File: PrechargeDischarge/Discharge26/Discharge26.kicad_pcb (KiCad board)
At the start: 2 copper layers, 80 x 105 mm, 11 parts, among them J1 HV_Conn, J2 LV_Conn, K4 Relay_SPST-NC, Q5 NMOS

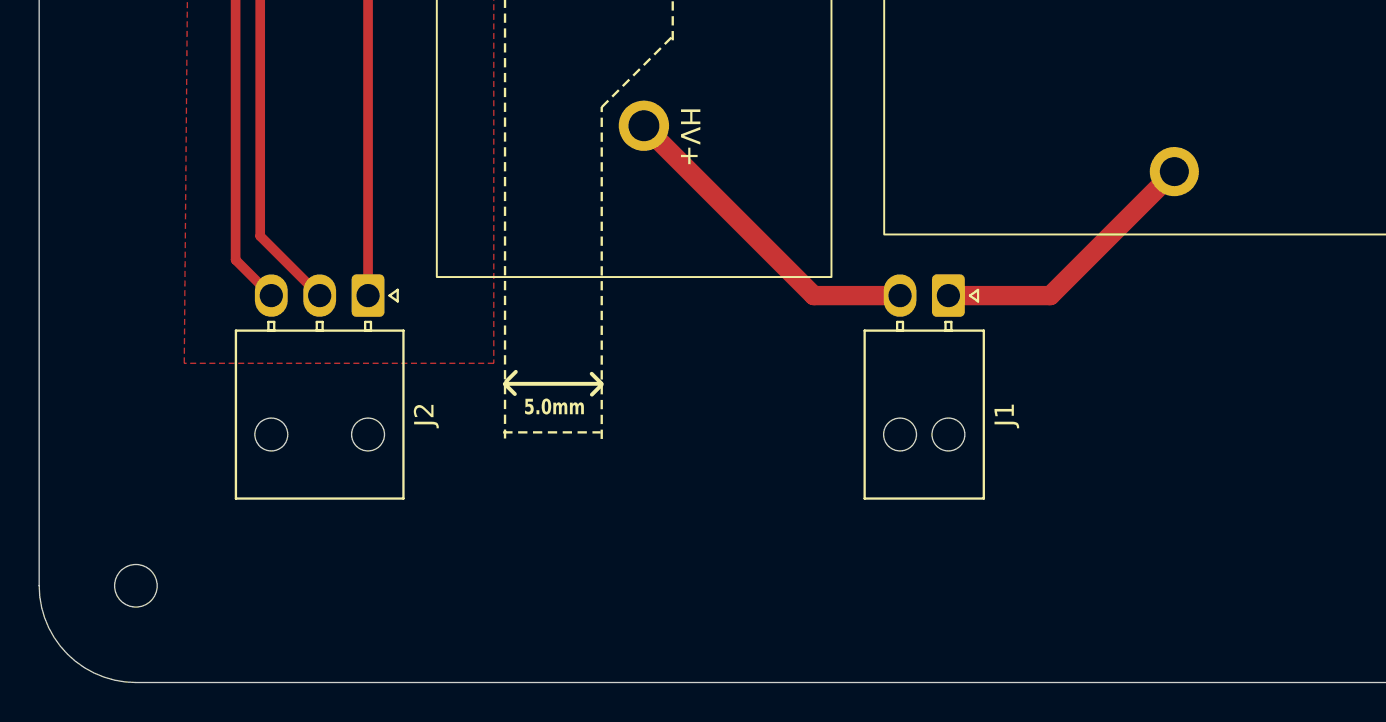
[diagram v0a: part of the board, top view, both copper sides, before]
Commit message: Precharge Testing
Uploaded precharge testing data, settled on 1.5k ohm resistor to precharge MC around 1s
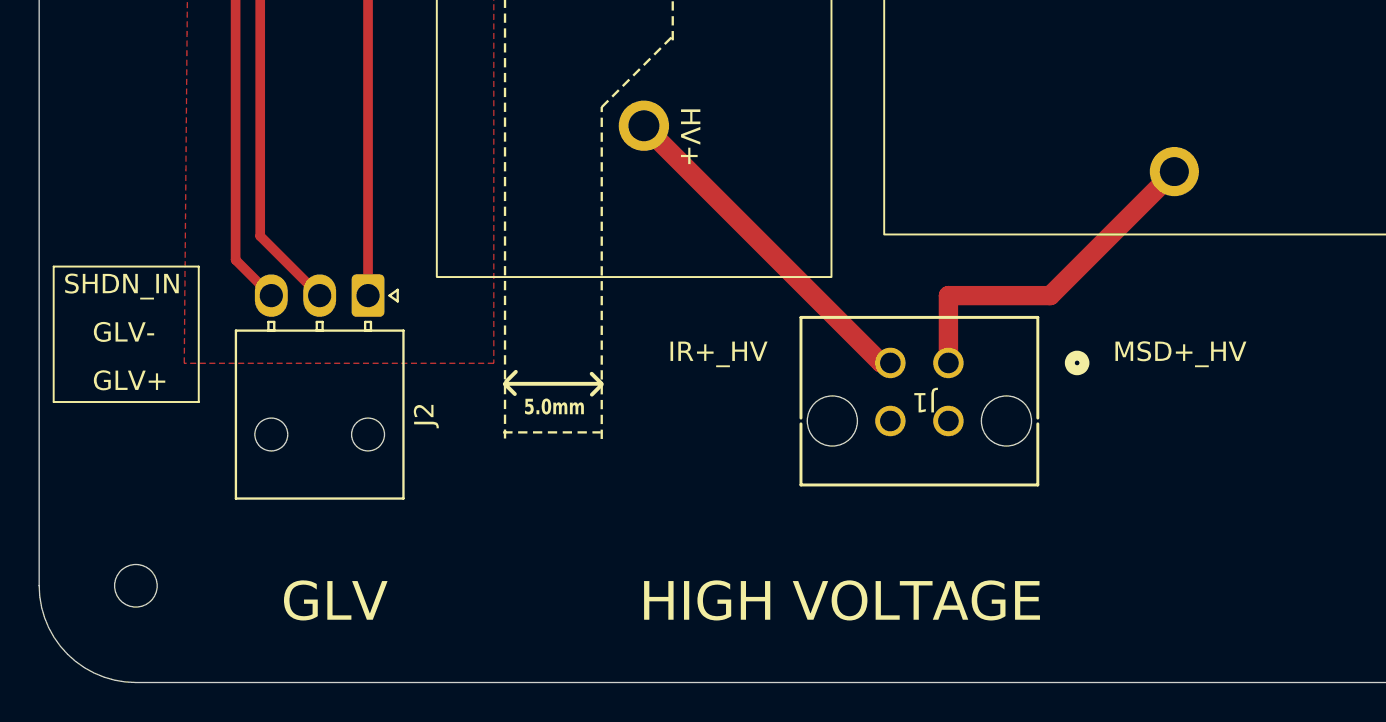
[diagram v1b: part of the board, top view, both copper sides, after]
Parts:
- J1: footprint Connector_Molex:Molex_Nano-Fit_105313-xx02_1x02_P2.50mm_Horizontal -> Discharge:MicroFit_4pin
- moved J1 5.15 mm to (170.7, 130.0), turned to 180 degrees
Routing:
- net /MSD_IN: track 14.3 -> 17.8 mm
- net /IR+: track 16.9 -> 17.8 mm
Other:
- board text added: "GLV"
- board text added: "GLV+"
- board text added: "GLV-"
- board text added: "HIGH VOLTAGE"
- board text added: "IR+_HV"
- board text added: "MSD+_HV"
- board text added: "SHDN_IN"

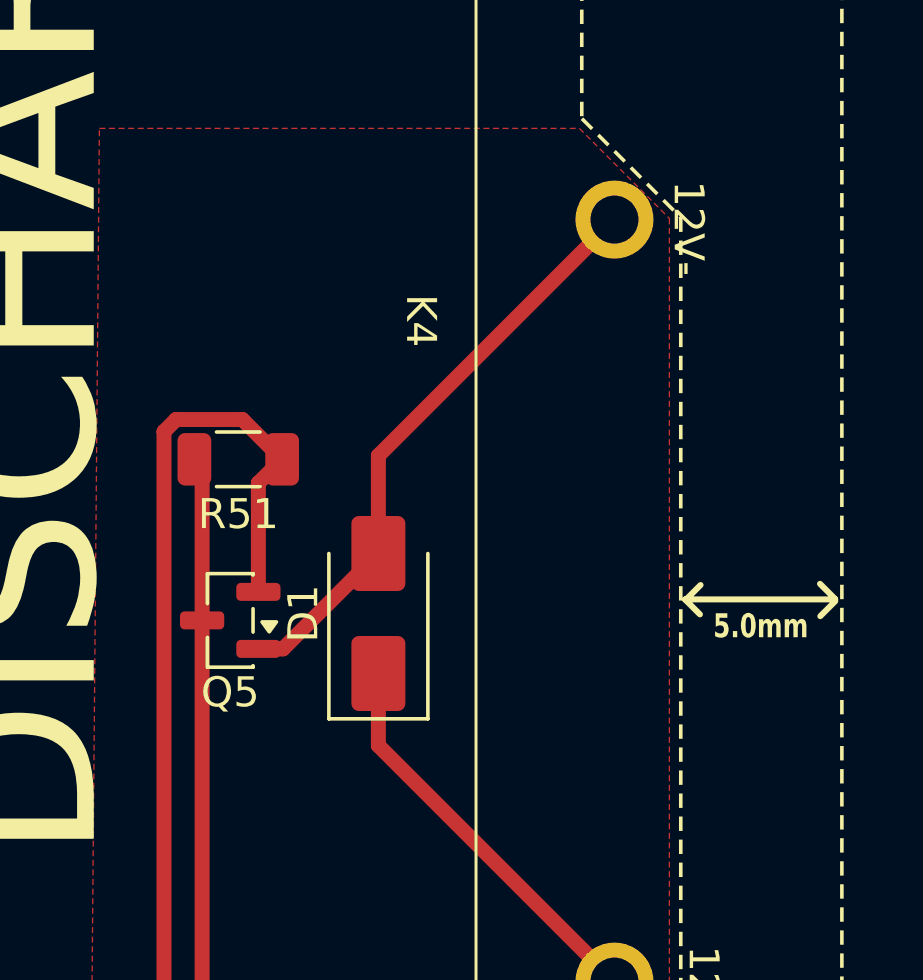
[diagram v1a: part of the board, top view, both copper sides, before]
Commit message: Discharge fixes
Fixed footprint and symbol for discharge NMOS
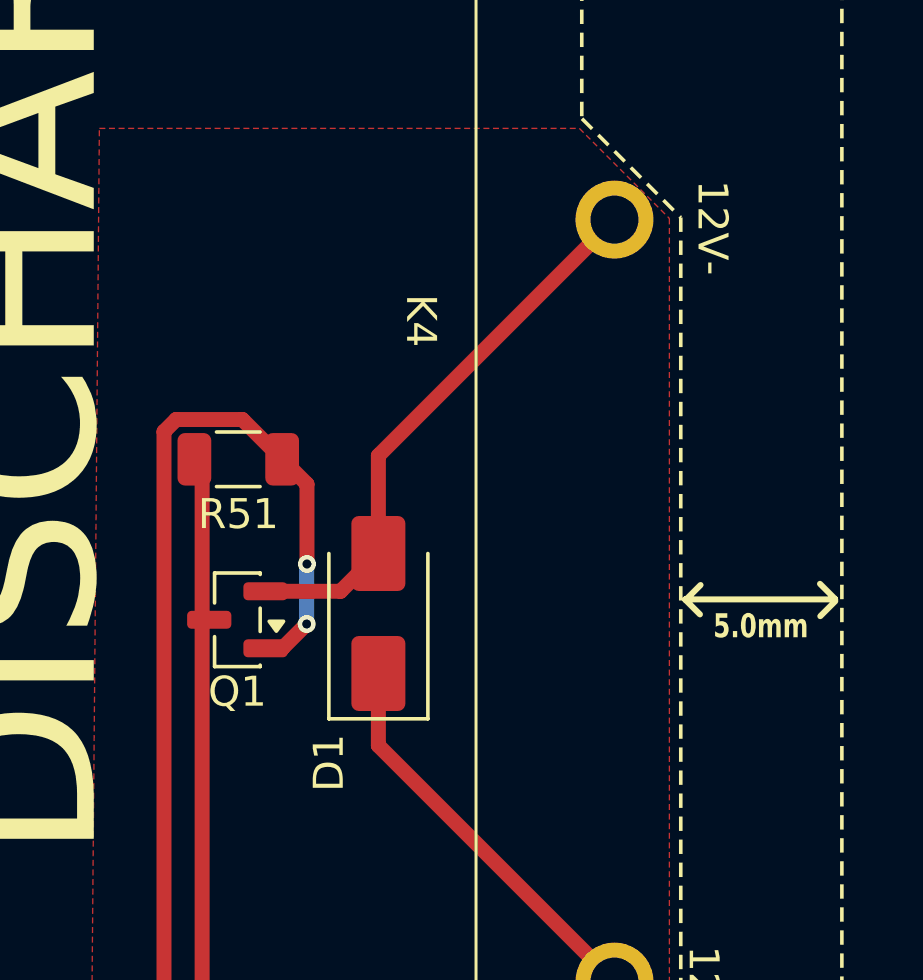
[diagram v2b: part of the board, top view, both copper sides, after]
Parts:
- removed Q5: NMOS, Package_TO_SOT_SMD:SOT-23
- added Q1: Q_NMOS_GSD, Package_TO_SOT_SMD:SOT-23, F.Cu at (137.6, 86.4)
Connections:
- J1 pad 3: (no net) -> unconnected-(J1-Pin_3-Pad3)
- J1 pad 4: (no net) -> unconnected-(J1-Pin_4-Pad4)
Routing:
- net /SHDN: track 55.1 -> 57.9 mm, vias 0 -> 2
- net Net-(D1-A): track 19.7 -> 18.7 mm

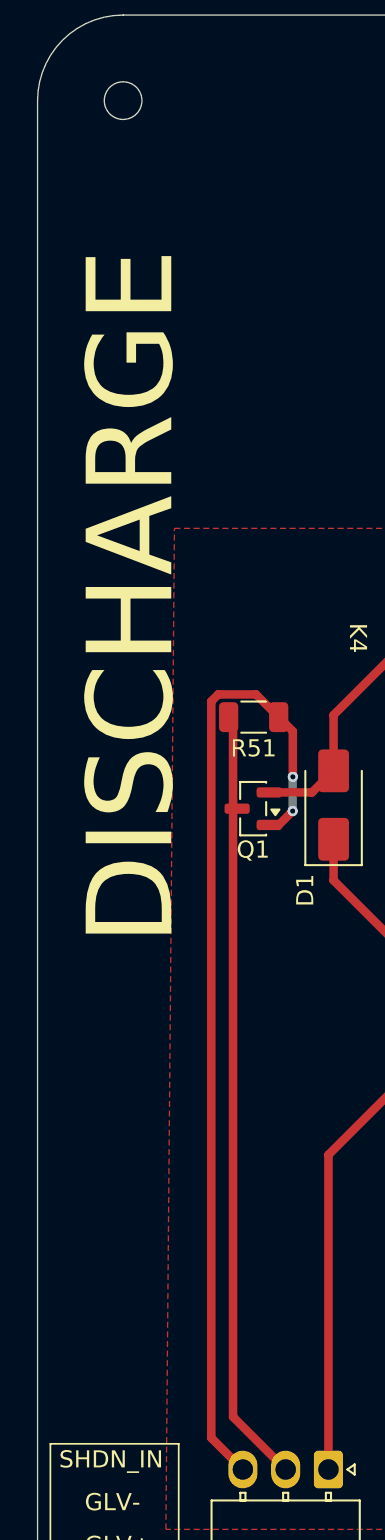
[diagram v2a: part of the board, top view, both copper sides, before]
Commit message: prechaarge
fixed precharge footprin
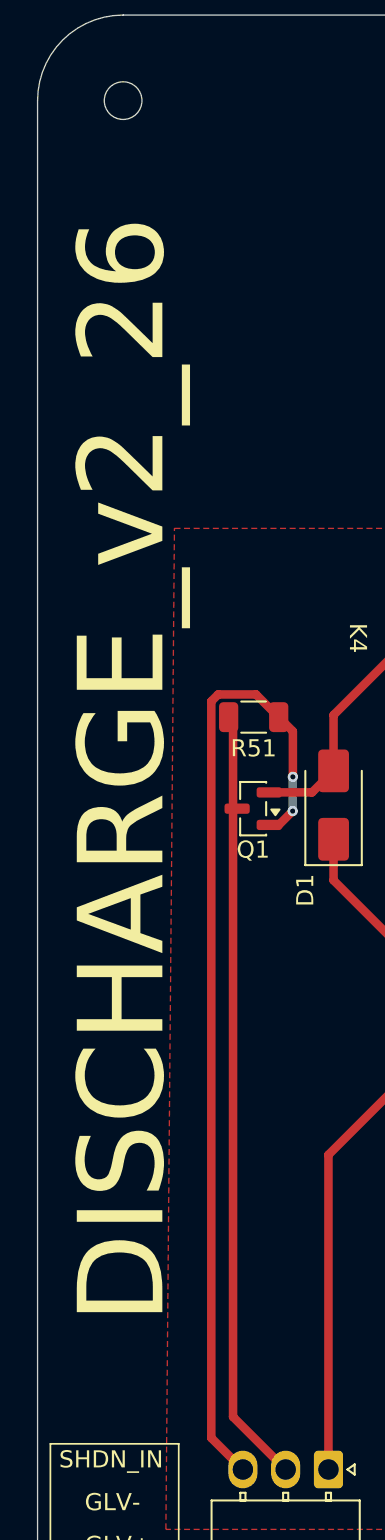
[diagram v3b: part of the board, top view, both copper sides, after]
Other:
- board text added: "DISCHARGE_v2_26"
- board text removed: "DISCHARGE"
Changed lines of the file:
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@@
 		)
 	)
-	(gr_text "DISCHARGE"
-		(at 130.5 74 90)
+	(gr_text "DISCHARGE_v2_26"
+		(at 129.98 84.12 90)
 		(layer "F.SilkS")
 		(effects

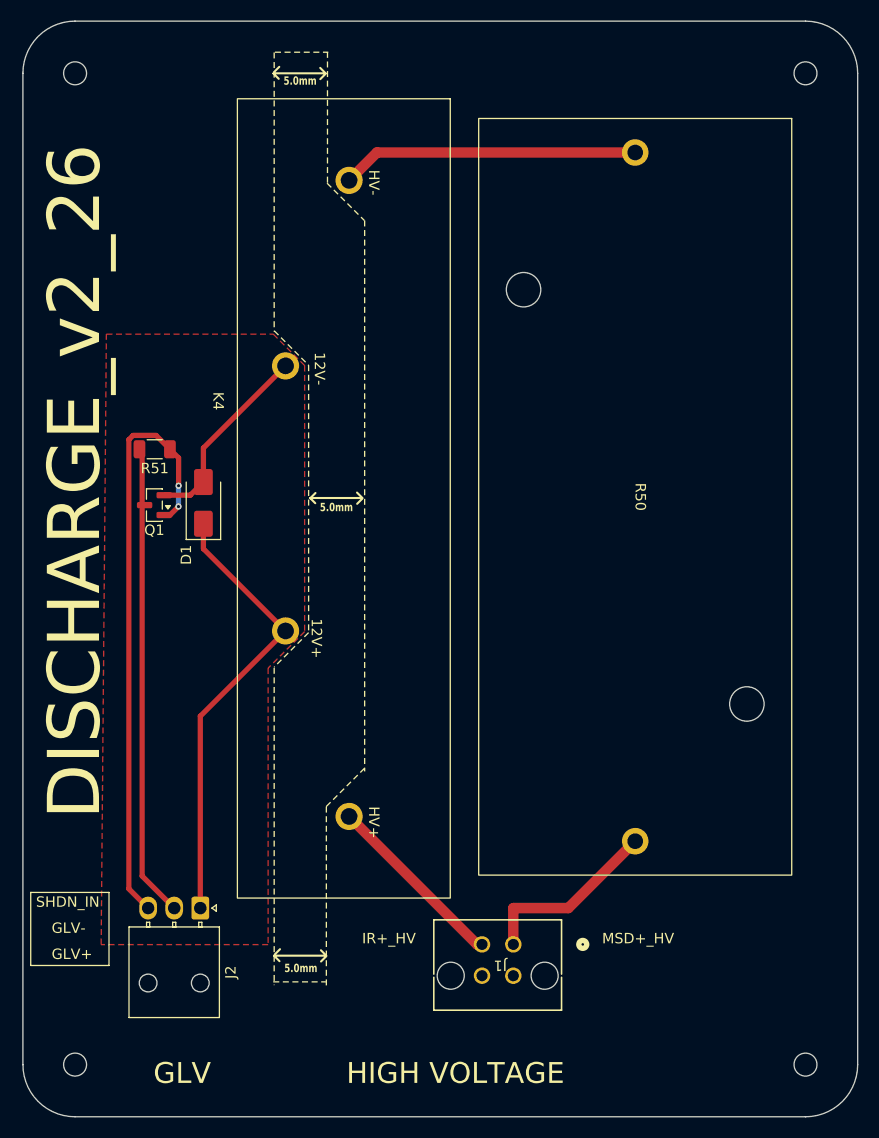
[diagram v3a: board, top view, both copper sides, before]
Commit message: Fixed Discharge NMOS
Drain was connected to ground
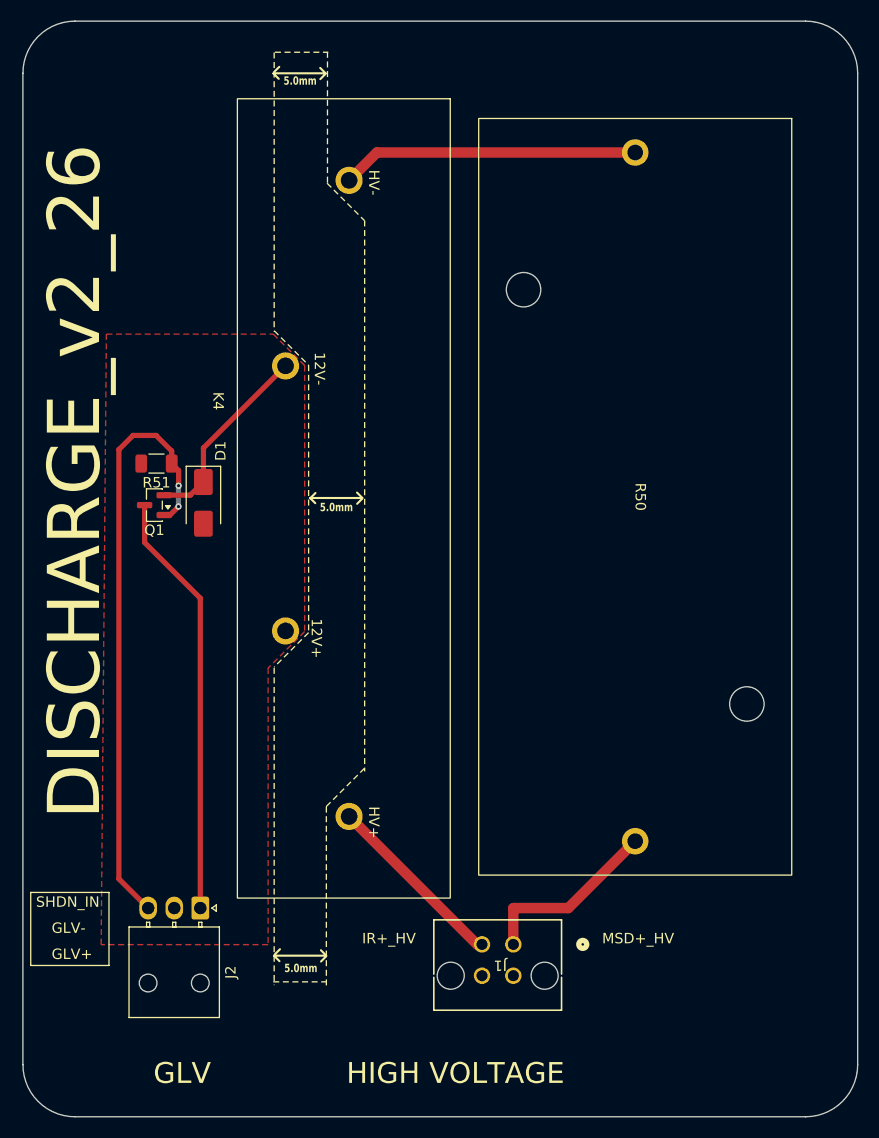
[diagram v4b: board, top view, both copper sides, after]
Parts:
- removed REF** (x4): MountingHole_2.2mm_M2, MountingHole:MountingHole_2.2mm_M2
- moved R51 1.38 mm to (137.8, 82.4)
- turned D1 to -90 degrees
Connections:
- D1 pad 1: GLV+ -> Net-(D1-K)
- D1 pad 2: Net-(D1-A) -> GND
- J2 pad 1: GLV+ -> +12V
- J2 pad 2: GLV- -> GND
- K4 pad 2: GLV+ -> GND
- K4 pad 5: Net-(D1-A) -> Net-(D1-K)
- Q1 pad 2: Net-(D1-A) -> Net-(D1-K)
- Q1 pad 3: GLV- -> +12V
- R51 pad 2: GLV- -> GND
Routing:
- net GLV-: track 45.4 -> 0.00 mm
- net GLV+: track 43.5 -> 0.00 mm
- net +12V: track 0.00 -> 40.8 mm
- net Net-(D1-K): track 0.00 -> 18.7 mm
- net Net-(D1-A): track 18.7 -> 0.00 mm
- net /SHDN: track 57.9 -> 58.6 mm
- added copper zone on F.Cu, net GND
- removed copper zone on F.Cu, net GLV-

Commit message: Discharge
guys its gonns work this time
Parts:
- added H1: MountingHole, MountingHole:MountingHole_2.2mm_M2, F.Cu at (130.0, 45.0)
- added H2: MountingHole, MountingHole:MountingHole_2.2mm_M2, F.Cu at (200.0, 45.0)
- added H3: MountingHole, MountingHole:MountingHole_2.2mm_M2, F.Cu at (200.0, 140.0)
- added H4: MountingHole, MountingHole:MountingHole_2.2mm_M2, F.Cu at (130.0, 140.0)
- moved D1 4.84 mm to (142.0, 91.0), turned to 90 degrees
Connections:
- D1 pad 1: Net-(D1-K) -> +12V
- D1 pad 2: GND -> Net-(D1-A)
- K4 pad 2: GND -> +12V
- K4 pad 5: Net-(D1-K) -> Net-(D1-A)
- Q1 pad 2: Net-(D1-K) -> GND
- Q1 pad 3: +12V -> Net-(D1-A)
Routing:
- net Net-(D1-A): track 0.00 -> 26.5 mm
- net Net-(D1-K): track 18.7 -> 0.00 mm
- net GND: track 0.00 -> 3.94 mm
- net /SHDN: track 58.6 -> 59.0 mm, vias 2 -> 0
- net (no net): vias 0 -> 17
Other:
- board text added: "DISCHARGE_v3_26"
- board text added: "GLV+(R)"
- board text added: "SHDN_IN(L)"
- board text removed: "DISCHARGE_v2_26"
- board text removed: "GLV+"
- board text removed: "SHDN_IN"
